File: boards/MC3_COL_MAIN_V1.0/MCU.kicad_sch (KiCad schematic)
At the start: 47 parts, among them J2 SWD, SW1 SKRKAEE020, U10 GP1S094HCZ0F, U11 GP1S094HCZ0F, U2 STM32F412RET6, U9 AEDR-8300-1Q0, Y1 8MHz

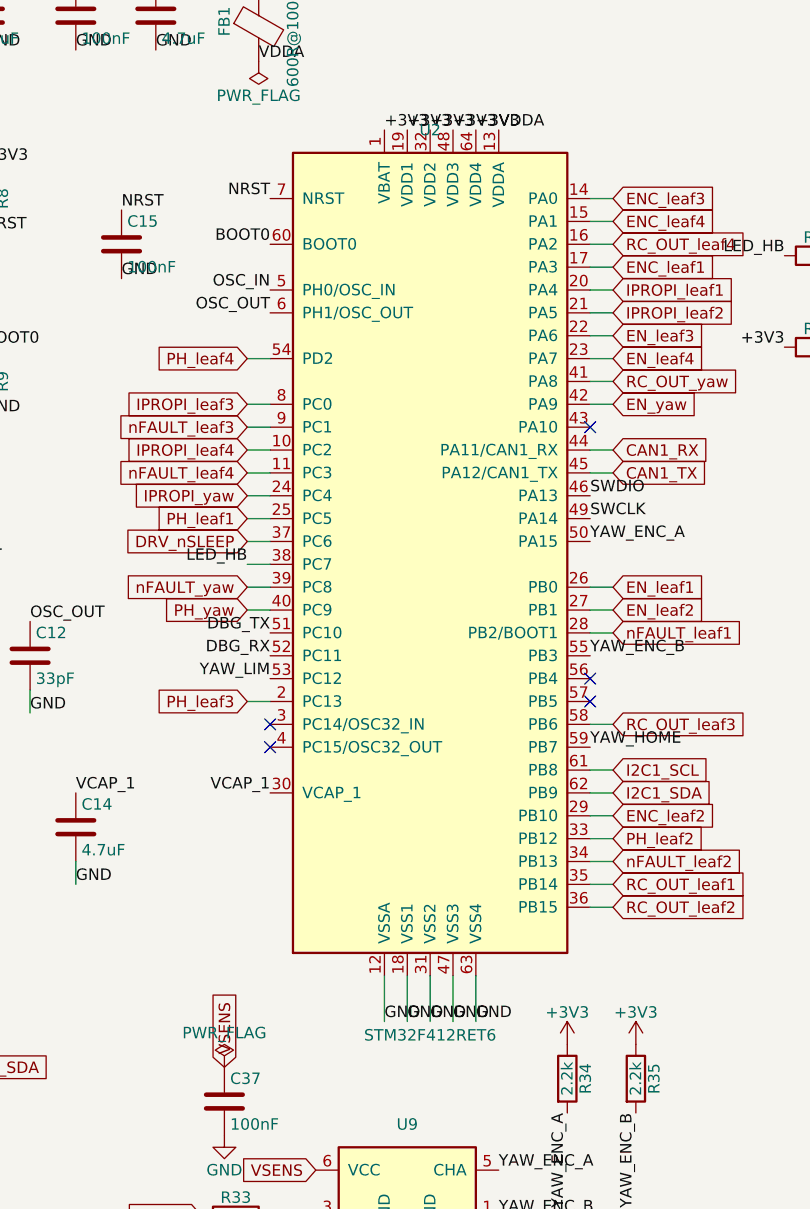
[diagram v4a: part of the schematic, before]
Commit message: MCU swap: STM32F412RET6 -> STM32U595RJT6 (non-Q, DigiKey) - copper-free; symbol cloned pin-exact, netlist diff clean (64/64 identical nets); COL-COTS-0035, 0029 superseded
Co-Authored-By: Claude Fable 5 <noreply@anthropic.com>
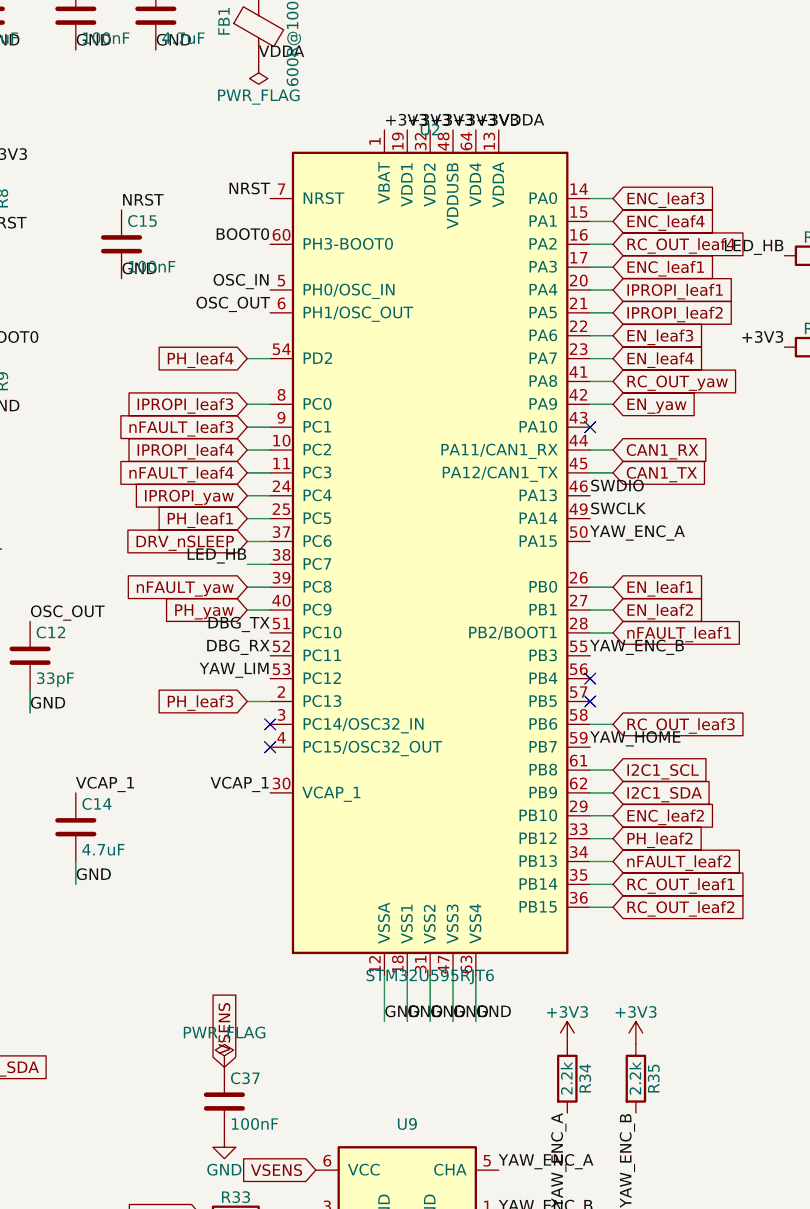
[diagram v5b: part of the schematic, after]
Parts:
- removed U2: STM32F412RET6, MC3_COL_MAIN:LQFP-64_10x10mm_P0.5mm, symbol MC3_COL_MAIN:STM32F412RET6
- added U2: STM32U595RJT6, MC3_COL_MAIN:LQFP-64_10x10mm_P0.5mm, symbol MC3_COL_MAIN:STM32U595RJT6
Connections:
- net +3V3: now also U2.1 (VBAT), U2.19 (VDD1), U2.32 (VDD2), U2.48 (VDDUSB), U2.64 (VDD4)
- net BOOT0: now also U2.60 (PH3-BOOT0)
- net CAN1_RX: now also U2.44 (PA11/CAN1_RX)
- net CAN1_TX: now also U2.45 (PA12/CAN1_TX)
- net DBG_RX: now also U2.52 (PC11)
- net DBG_TX: now also U2.51 (PC10)
- net DRV_nSLEEP: now also U2.37 (PC6)
- net ENC_leaf1: now also U2.17 (PA3)
- net ENC_leaf2: now also U2.29 (PB10)
- net ENC_leaf3: now also U2.14 (PA0)
- net ENC_leaf4: now also U2.15 (PA1)
- net EN_leaf1: now also U2.26 (PB0)
- net EN_leaf2: now also U2.27 (PB1)
- net EN_leaf3: now also U2.22 (PA6)
- net EN_leaf4: now also U2.23 (PA7)
- net EN_yaw: now also U2.42 (PA9)
- net GND: now also U2.12 (VSSA), U2.18 (VSS1), U2.31 (VSS2), U2.47 (VSS3), U2.63 (VSS4)
- net I2C1_SCL: now also U2.61 (PB8)
- net I2C1_SDA: now also U2.62 (PB9)
- net IPROPI_leaf1: now also U2.20 (PA4)
- net IPROPI_leaf2: now also U2.21 (PA5)
- net IPROPI_leaf3: now also U2.8 (PC0)
- net IPROPI_leaf4: now also U2.10 (PC2)
- net IPROPI_yaw: now also U2.24 (PC4)
- net LED_HB: now also U2.38 (PC7)
- net NRST: now also U2.7 (NRST)
- net OSC_IN: now also U2.5 (PH0/OSC_IN)
- net OSC_OUT: now also U2.6 (PH1/OSC_OUT)
- net PH_leaf1: now also U2.25 (PC5)
- net PH_leaf2: now also U2.33 (PB12)
- net PH_leaf3: now also U2.2 (PC13)
- net PH_leaf4: now also U2.54 (PD2)
- net PH_yaw: now also U2.40 (PC9)
- net RC_OUT_leaf1: now also U2.35 (PB14)
- net RC_OUT_leaf2: now also U2.36 (PB15)
- net RC_OUT_leaf3: now also U2.58 (PB6)
- net RC_OUT_leaf4: now also U2.16 (PA2)
- net RC_OUT_yaw: now also U2.41 (PA8)
- net SWCLK: now also U2.49 (PA14)
- net SWDIO: now also U2.46 (PA13)
- net VCAP_1: now also U2.30 (VCAP_1)
- net VDDA: now also U2.13 (VDDA)
- net YAW_ENC_A: now also U2.50 (PA15)
- net YAW_ENC_B: now also U2.55 (PB3)
- net YAW_HOME: now also U2.59 (PB7)
- net YAW_LIM: now also U2.53 (PC12)
- net nFAULT_leaf1: now also U2.28 (PB2/BOOT1)
- net nFAULT_leaf2: now also U2.34 (PB13)
- net nFAULT_leaf3: now also U2.9 (PC1)
- net nFAULT_leaf4: now also U2.11 (PC3)
- net nFAULT_yaw: now also U2.39 (PC8)
